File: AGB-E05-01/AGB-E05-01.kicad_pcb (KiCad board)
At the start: 2 copper layers, 51 x 31 mm, 24 parts, among them U0 CartBus, U1 R27V12813M, U2 LE26FV10N1TS, U3 S3511, X1 Crystal_GND2

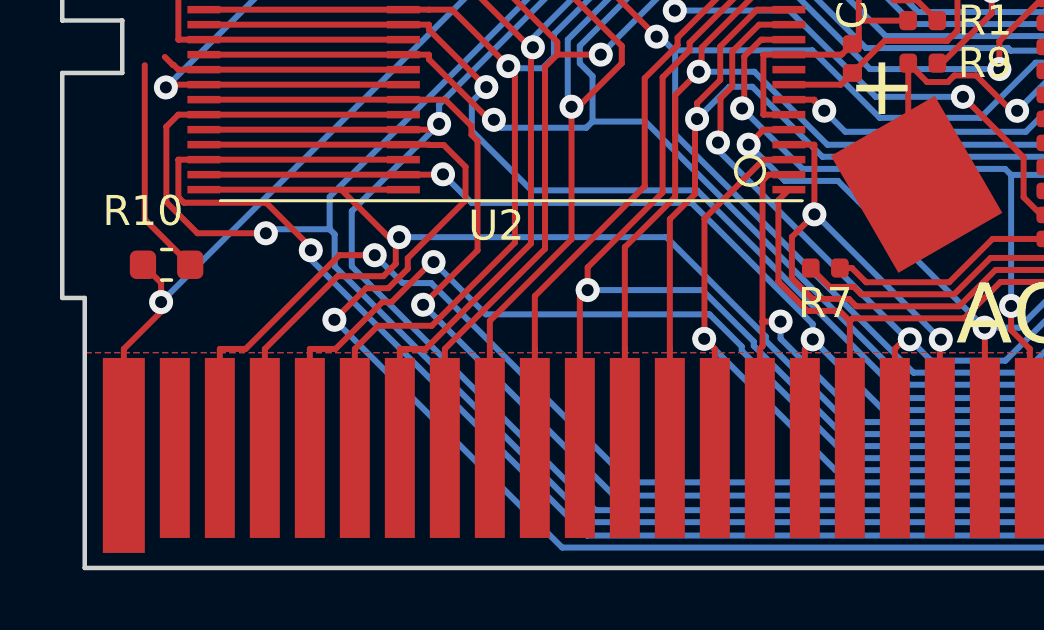
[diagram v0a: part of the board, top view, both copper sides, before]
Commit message: Move R7 and R10 up
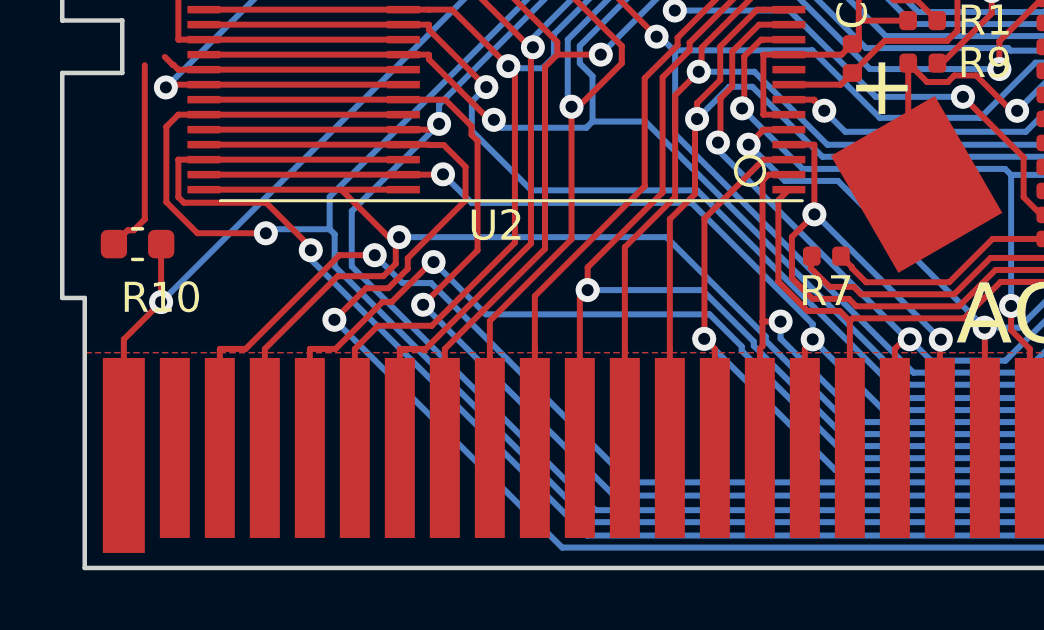
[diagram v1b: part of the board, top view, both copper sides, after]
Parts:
- moved R10 1.19 mm to (129.3, 90.9), turned to 180 degrees
- moved R7 0.40 mm to (152.3, 91.3)
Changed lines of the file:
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@@
     (thickness 0.8)
     (drawings 21)
-    (tracks 932)
+    (tracks 937)
     (zones 0)
     (modules 24)
@@
   )
   (module Resistor_SMD:R_0402_1005Metric (layer F.Cu)
-    (at 152.273 91.6686 180)
+    (at 152.30856 91.27236 180)
     (descr "Resistor SMD 0402 (1005 Metric), square (rectangular) end terminal, IPC_7351 nominal, (Body size source: http://www.tortai-tech.com/upload/download/2011102023233369053.pdf), generated with kicad-footprint-generator")
     (tags resistor)
@@
   )
   (module Resistor_SMD:R_0603_1608Metric (layer F.Cu)
-    (at 130.315 91.5594)
+    (at 129.34696 90.87104 180)
     (descr "Resistor SMD 0603 (1608 Metric), square (rectangular) end terminal, IPC_7351 nominal, (Body size source: http://www.tortai-tech.com/upload/download/2011102023233369053.pdf), generated with kicad-footprint-generator")
     (tags resistor)
@@
       (effects (font (size 0.4 0.4) (thickness 0.06)))
     )
-    (pad 1 smd roundrect (at -0.7875 0) (size 0.875 0.95) (layers F.Cu F.Paste F.Mask) (roundrect_rratio 0.25)
+    (pad 1 smd roundrect (at -0.7875 0 180) (size 0.875 0.95) (layers F.Cu F.Paste F.Mask) (roundrect_rratio 0.25)
       (net 2 +3V3))
-    (pad 2 smd roundrect (at 0.7875 0) (size 0.875 0.95) (layers F.Cu F.Paste F.Mask) (roundrect_rratio 0.25)
+    (pad 2 smd roundrect (at 0.7875 0 180) (size 0.875 0.95) (layers F.Cu F.Paste F.Mask) (roundrect_rratio 0.25)
       (net 3 GND))
     (model ${KISYS3DMOD}/Resistor_SMD.3dshapes/R_0603_1608Metric.wrl
@@
   (segment (start 174.9866 87.2122) (end 174.9866 86.5417) (width 0.2) (layer F.Cu) (net 2))
   (segment (start 173.1003 89.0985) (end 174.9866 87.2122) (width 0.2) (layer F.Cu) (net 2))
-  (via (at 130.1324 92.8035) (size 0.8) (layers F.Cu B.Cu) (net 2))
   (via (at 151.1529 78.7172) (size 0.8) (layers F.Cu B.Cu) (net 2))
   (segment (start 172.7522 80.4157) (end 171.835 79.4985) (width 0.2) (layer F.Cu) (net 2))
   (segment (start 171.835 79.4985) (end 171.2465 79.4985) (width 0.2) (layer F.Cu) (net 2))
   (segment (start 151.8482 78.7172) (end 151.1529 78.7172) (width 0.2) (layer F.Cu) (net 2))
-  (segment (start 130.1324 92.8035) (end 130.1324 92.1643) (width 0.2) (layer F.Cu) (net 2))
   (segment (start 157.902 77.0694) (end 157.2993 77.0694) (width 0.2) (layer F.Cu) (net 2))
   (segment (start 156.6772 83.7534) (end 156.3329 84.0977) (width 0.2) (layer F.Cu) (net 2))
@@
   (segment (start 159.4729 75.4985) (end 157.902 77.0694) (width 0.2) (layer F.Cu) (net 2))
   (segment (start 160.0715 80.2985) (end 163.7891 80.2985) (width 0.2) (layer F.Cu) (net 2))
-  (segment (start 128.89 97.9158) (end 128.89 94.3655) (width 0.2) (layer F.Cu) (net 2))
   (segment (start 144.0801 78.8558) (end 130.1324 92.8035) (width 0.2) (layer B.Cu) (net 2))
   (segment (start 151.1529 78.7172) (end 151.0143 78.8558) (width 0.2) (layer B.Cu) (net 2))
-  (segment (start 130.1324 92.1643) (end 129.5275 91.5594) (width 0.2) (layer F.Cu) (net 2))
-  (segment (start 130.1324 93.1231) (end 128.89 94.3655) (width 0.2) (layer F.Cu) (net 2))
-  (segment (start 130.1324 92.8035) (end 130.1324 93.1231) (width 0.2) (layer F.Cu) (net 2))
   (segment (start 157.8673 81.7341) (end 157.5316 81.7341) (width 0.2) (layer F.Cu) (net 2))
   (segment (start 157.2993 77.0694) (end 156.7735 77.5952) (width 0.2) (layer F.Cu) (net 2))
+  (segment (start 130.1324 92.8035) (end 130.1324 92.8035) (width 0.2) (layer B.Cu) (net 2))
+  (via (at 130.1324 92.8035) (size 0.8) (drill 0.4) (layers F.Cu B.Cu) (net 2))
+  (segment (start 128.89 94.0459) (end 130.1324 92.8035) (width 0.2) (layer F.Cu) (net 2))
+  (segment (start 128.89 97.9158) (end 128.89 94.0459) (width 0.2) (layer F.Cu) (net 2))
+  (segment (start 130.1324 90.8731) (end 130.13446 90.87104) (width 0.2) (layer F.Cu) (net 2))
+  (segment (start 130.1324 92.8035) (end 130.1324 90.8731) (width 0.2) (layer F.Cu) (net 2))
   (segment (start 135.811 74.4931) (end 135.0356 75.2685) (width 0.2) (layer F.Cu) (net 3))
   (segment (start 150.2565 79.4697) (end 151.662 79.4697) (width 0.2) (layer F.Cu) (net 3))
@@
   (segment (start 154.694 81.0043) (end 154.694 80.4951) (width 0.2) (layer F.Cu) (net 3))
   (segment (start 150.18258 74.51344) (end 150.17496 74.51344) (width 0.2) (layer F.Cu) (net 3))
-  (segment (start 129.5877 90.0446) (end 131.1025 91.5594) (width 0.2) (layer F.Cu) (net 3))
   (segment (start 150.26032 74.6262) (end 150.26032 74.59118) (width 0.2) (layer F.Cu) (net 3))
   (segment (start 175.061087 77.4791) (end 175.061087 82.880113) (width 0.2) (layer F.Cu) (net 3))
@@
   (segment (start 150.167 77.1778) (end 149.972 76.9828) (width 0.2) (layer F.Cu) (net 3))
   (segment (start 149.972 76.9828) (end 144.16992 76.9828) (width 0.2) (layer F.Cu) (net 3))
+  (segment (start 129.222872 90.409428) (end 129.5877 90.0446) (width 0.2) (layer F.Cu) (net 3))
+  (segment (start 129.021072 90.409428) (end 129.222872 90.409428) (width 0.2) (layer F.Cu) (net 3))
+  (segment (start 128.55946 90.87104) (end 129.021072 90.409428) (width 0.2) (layer F.Cu) (net 3))
+  (segment (start 151.788 91.30792) (end 151.82356 91.27236) (width 0.2) (layer F.Cu) (net 3))
+  (segment (start 151.788 91.6686) (end 151.788 91.30792) (width 0.2) (layer F.Cu) (net 3))
   (via (at 151.5968 75.8271) (size 0.8) (layers F.Cu B.Cu) (net 4))
   (via (at 157.8216 82.4344) (size 0.8) (layers F.Cu B.Cu) (net 4))
@@
   (segment (start 156.4024 92.1431) (end 153.6337 92.1431) (width 0.2) (layer F.Cu) (net 12))
   (segment (start 153.6337 92.1431) (end 153.1592 91.6686) (width 0.2) (layer F.Cu) (net 12))
-  (segment (start 153.1592 91.6686) (end 152.758 91.6686) (width 0.2) (layer F.Cu) (net 12))
+  (segment (start 153.1592 91.638) (end 152.79356 91.27236) (width 0.2) (layer F.Cu) (net 12))
+  (segment (start 153.1592 91.6686) (end 153.1592 91.638) (width 0.2) (layer F.Cu) (net 12))
   (segment (start 148.3232 77.7915) (end 151.4687 77.7915) (width 0.2) (layer F.Cu) (net 13))
   (segment (start 148.1185 77.5868) (end 148.3232 77.7915) (width 0.2) (layer F.Cu) (net 13))

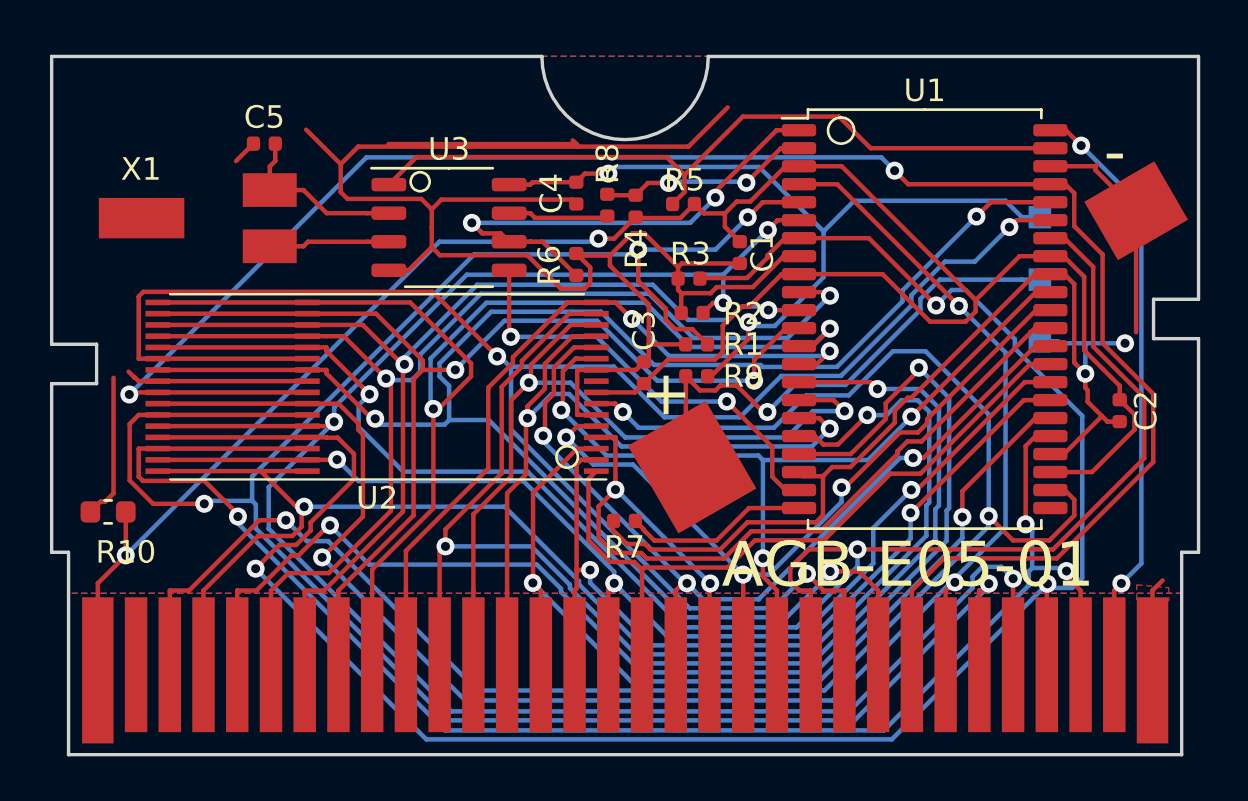
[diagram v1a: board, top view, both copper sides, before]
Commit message: Move battery pads slightly up
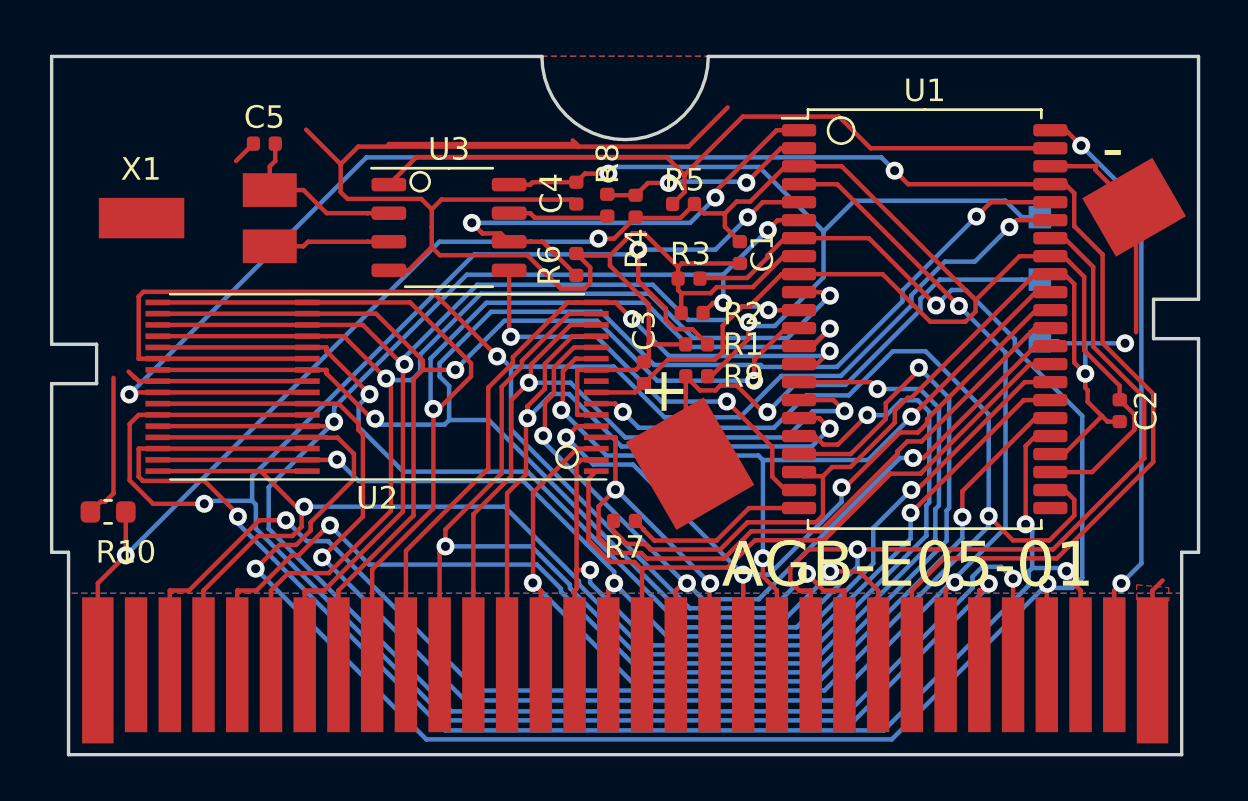
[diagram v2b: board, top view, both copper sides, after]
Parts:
- moved BT1 0.18 mm to (165.2, 83.0)
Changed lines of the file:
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@@
       (outputformat 1)
       (mirror false)
-      (drillshape 1)
+      (drillshape 0)
       (scaleselection 1)
-      (outputdirectory ""))
+      (outputdirectory "../Gerbers/"))
   )
   (net 0 "")
@@
   )
   (module NintendoFootprints:CR1616 (layer F.Cu)
-    (at 165.275 83.1291 30)
+    (at 165.186312 82.9722 30)
     (fp_text reference BT1 (at -0.07112 4.97078 30) (layer F.SilkS) hide
       (effects (font (size 1 1) (thickness 0.15)))

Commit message: Update AGB-E05-01
Moved bottom of screwpost cutout down slightly for better alignment,
moved all components up to make the pcb fit like it should inside the
original shell
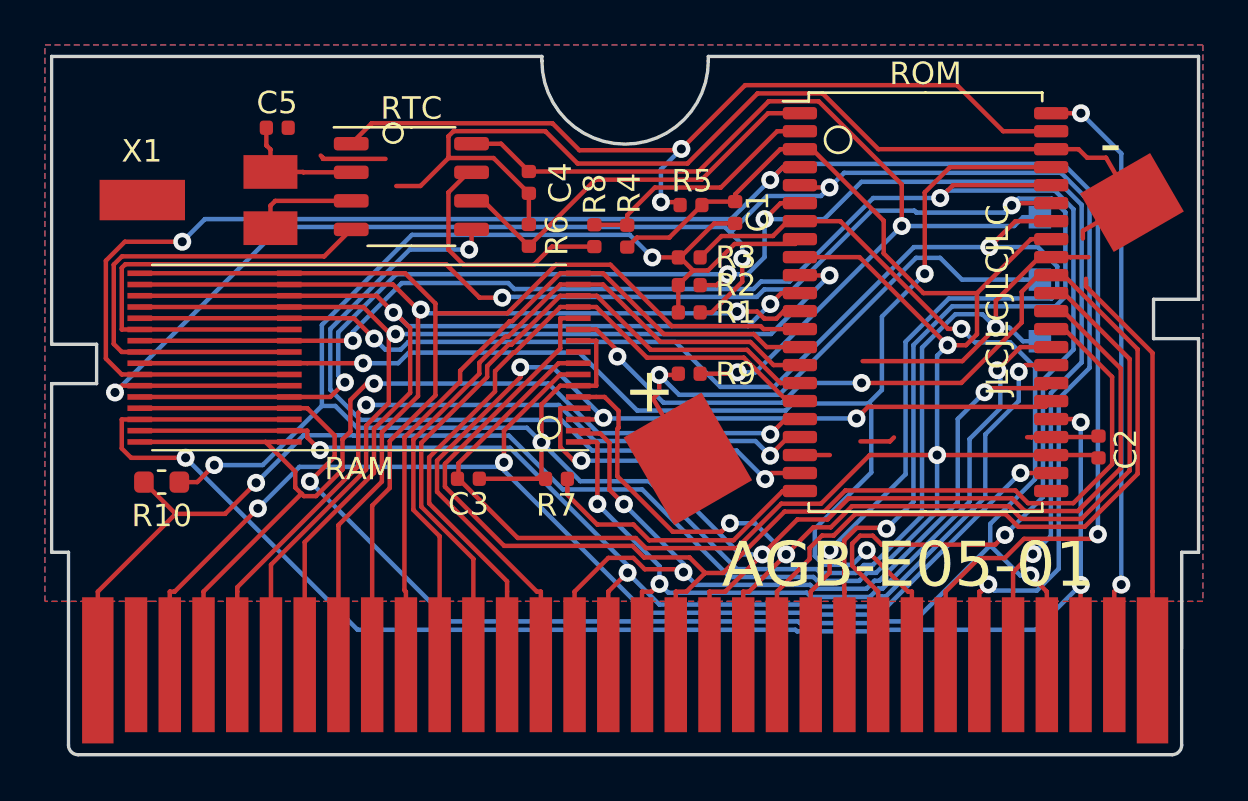
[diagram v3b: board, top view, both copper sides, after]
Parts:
- moved C3 9.12 mm to (145.4, 89.4), turned to 0 degrees
- moved R7 3.56 mm to (149.3, 89.4)
- moved R10 2.72 mm to (131.7, 89.5), turned to 0 degrees
- moved R6 2.47 mm to (148.1, 78.6)
- moved RTC 2.47 mm to (142.8, 76.4)
- moved C4 2.16 mm to (148.1, 76.2)
- moved C2 1.87 mm to (173.4, 88.0), turned to 90 degrees
- moved C1 1.79 mm to (157.2, 77.6)
- moved RAM 1.53 mm to (140.5, 84.0)
- moved R8 1.47 mm to (151.0, 78.6)
- moved R1 1.46 mm to (155.2, 82.0)
- moved R4 1.39 mm to (152.4, 78.6)
- moved R2 1.25 mm to (155.2, 80.8)
- moved R3 0.94 mm to (155.2, 79.6)
- moved C5 0.91 mm to (136.9, 73.8), turned to 180 degrees
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- renumbered U2 to RAM, U1 to ROM, U3 to RTC
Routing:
- net GND: track 161.8 -> 208.4 mm, vias 2 -> 4
- net +3V3: track 96.5 -> 133.5 mm, vias 2 -> 3
- net A5: track 58.1 -> 32.3 mm, vias 2 -> 0
- net WR: track 79.3 -> 56.1 mm
- net CS: track 57.0 -> 34.5 mm
- net A15: track 38.6 -> 58.6 mm, vias 3 -> 2
- net RD: track 64.2 -> 46.1 mm
- net D3: track 84.8 -> 66.9 mm, vias 2 -> 3
- net A12: track 39.8 -> 56.5 mm, vias 3 -> 0
- net RTC_CS: track 19.4 -> 33.9 mm
- net D7: track 92.1 -> 79.6 mm
- net A14: track 35.0 -> 47.0 mm, vias 3 -> 2
- net D4: track 76.4 -> 86.9 mm
- net D6: track 84.4 -> 74.0 mm
- net D5: track 96.8 -> 86.5 mm
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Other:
- board size 51 x 31 mm -> 51 x 31.1 mm
- net class Default: clearance 0.2 -> 0.15
- rule pad_to_mask_clearance: 0.051 -> 0.0508
- rule trace_clearance: 0.2 -> 0.15
- board text added: "JLCJLCJLCJLC"
